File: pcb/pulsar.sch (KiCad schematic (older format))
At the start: 74 parts, among them J1 Conn_01x04, K1 KEYSW, K2 KEYSW, K3 KEYSW, K4 KEYSW, K5 KEYSW, K6 KEYSW, K7 KEYSW, K8 KEYSW, K9 KEYSW, SW1 SW_PUSH, SW2 Rotary_Encoder, SW3 TMHU28, U1 ProMicro

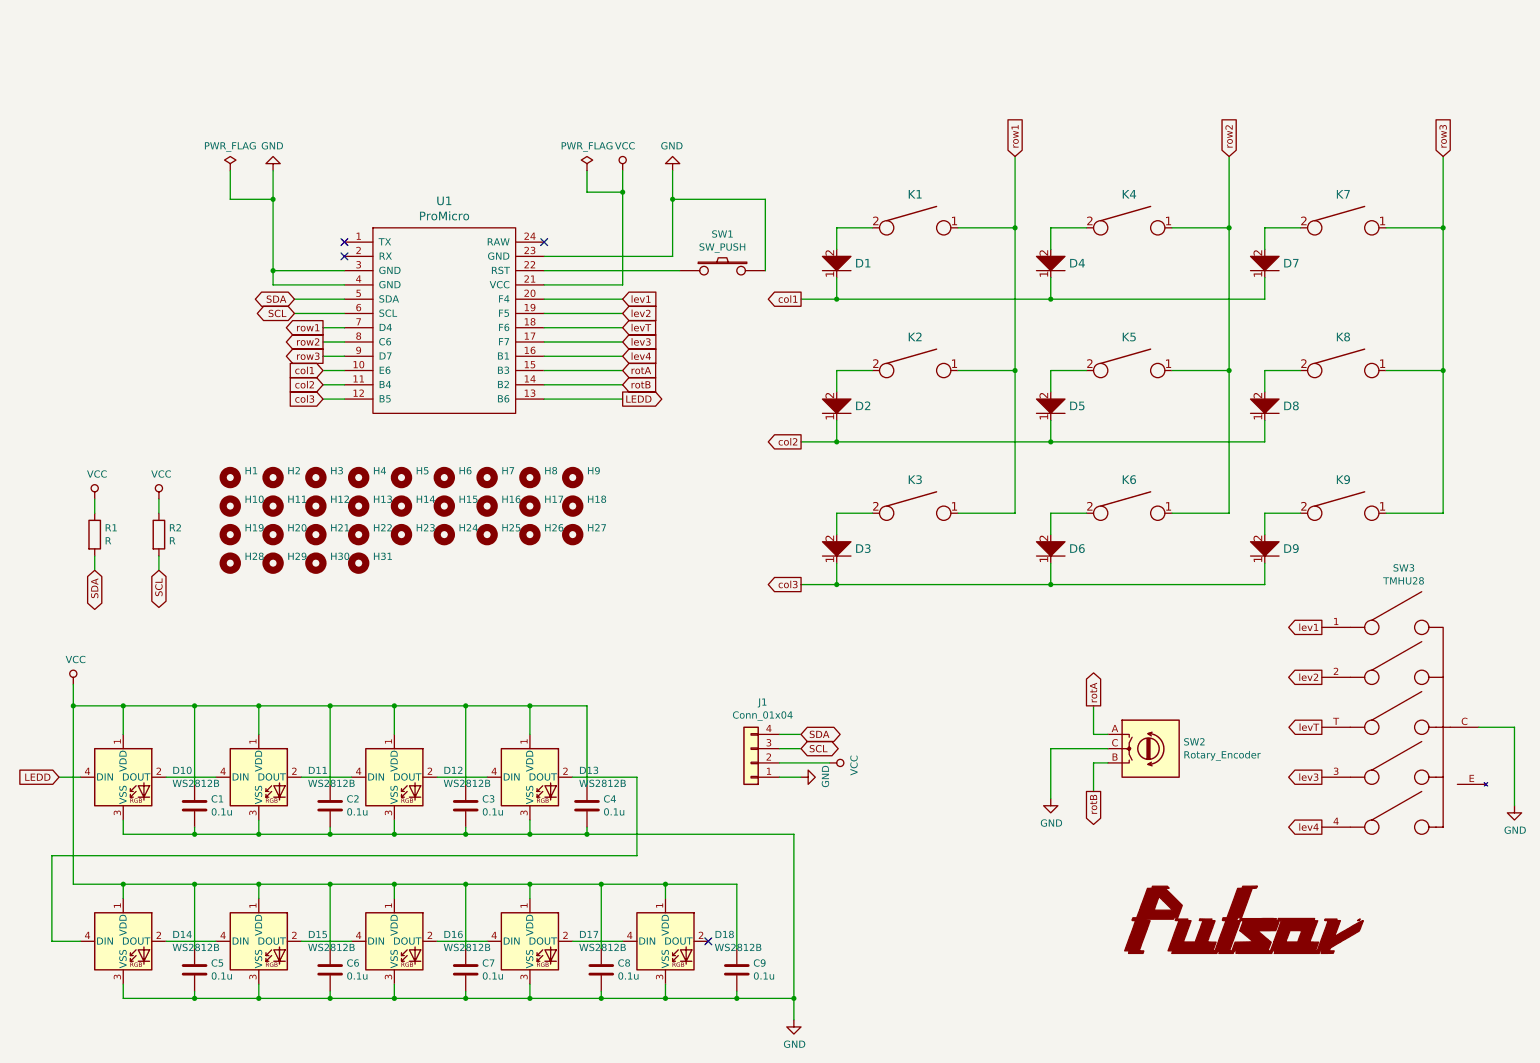
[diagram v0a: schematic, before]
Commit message: update pcb: rev2.0 - 11 keys
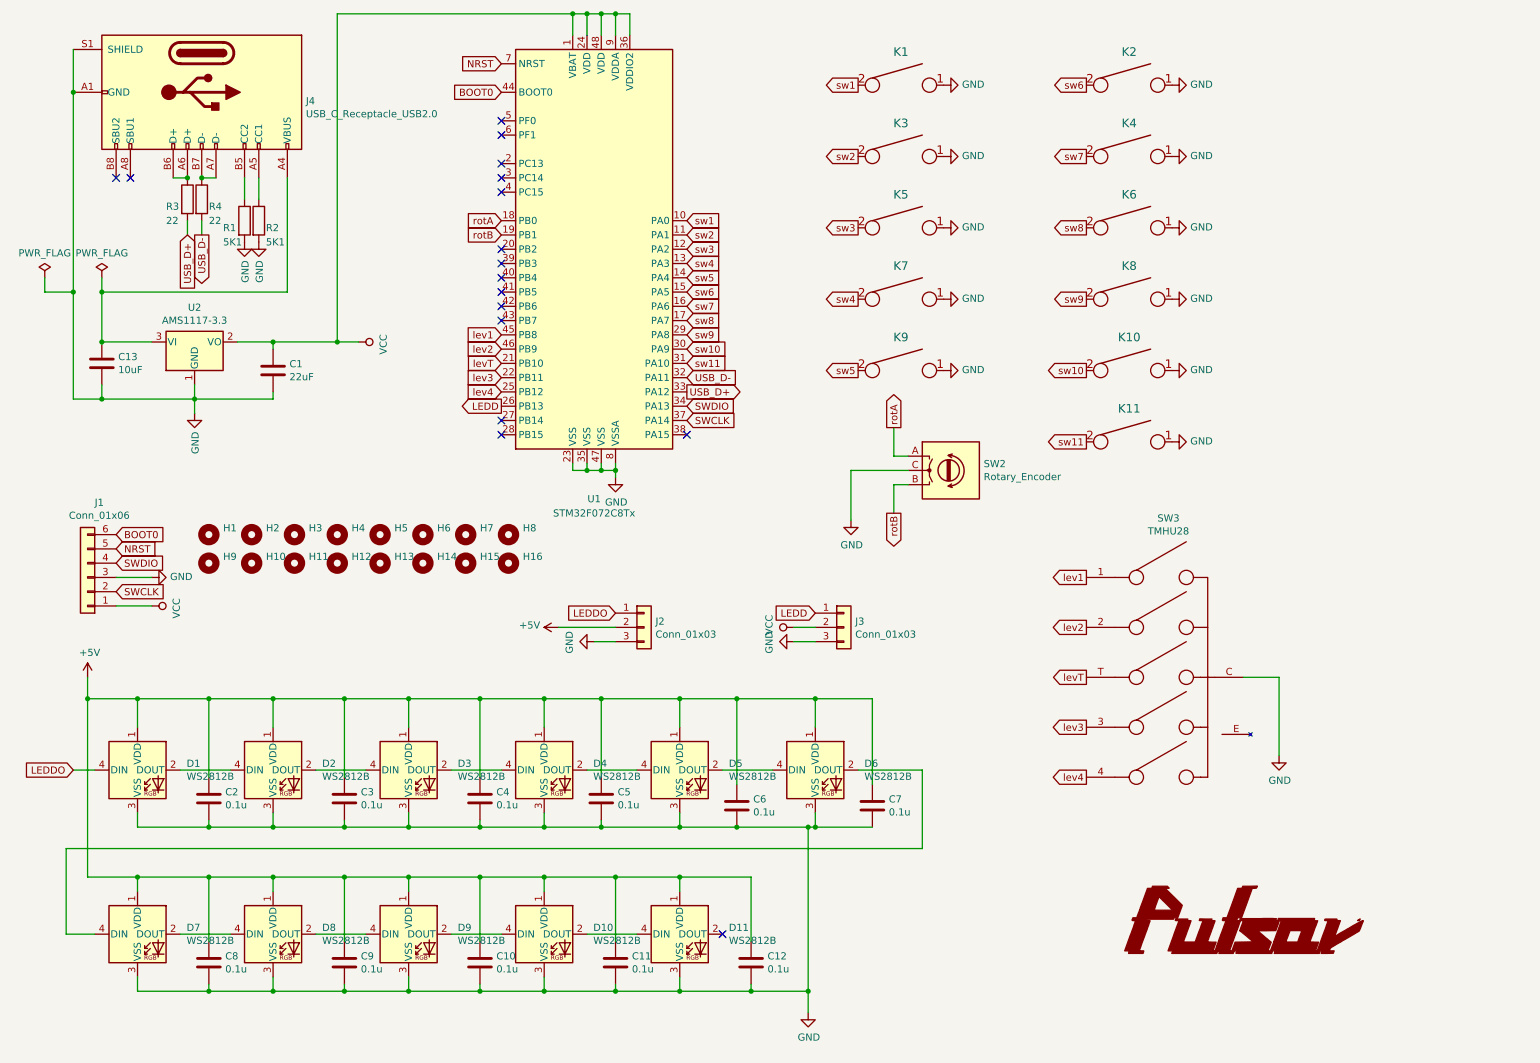
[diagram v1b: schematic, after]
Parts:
- removed D1, D2, D3, D4, D5, D6, D7, D8, D9: D, Diodes_SMD:D_SOD-123, symbol keyboard_parts:D
- removed D12, D13, D14, D15, D16, D17, D18: WS2812B, WS2812-2020:WS2812B-2020, symbol LED:WS2812B
- removed H17, H18, H19, H20, H21, H22, H23, H24, H25, H26, H27, H28, H29, H30, H31: MountingHole, Mounting_Holes:MountingHole_2.2mm_M2, symbol Mechanical:MountingHole
- removed J1: Conn_01x04, Pin_Headers:Pin_Header_Straight_1x04_Pitch2.54mm, symbol Connector_Generic:Conn_01x04
- removed SW1: SW_PUSH, pluser:tactswitch-2lead-6mm, symbol keyboard_parts:SW_PUSH
- removed U1: ProMicro, Keebio-Parts:ArduinoProMicro-ZigZag, symbol promicro:ProMicro
- added C10, C11, C12: 0.1u, Capacitors_SMD:C_0805_HandSoldering, symbol Device:C
- added C13: 10uF, Capacitors_SMD:C_0805_HandSoldering, symbol Device:C
- added D1, D2, D3, D4, D5, D6, D7, D8, D9: WS2812B, LED_SMD:LED_SK6812MINI_PLCC4_3.5x3.5mm_P1.75mm, symbol LED:WS2812B
- added J1: Conn_01x06, Pin_Headers:Pin_Header_Straight_1x06_Pitch2.54mm, symbol Connector_Generic:Conn_01x06
- added J2: Conn_01x03, Pin_Headers:Pin_Header_Straight_1x03_Pitch2.54mm_SMD_Pin1Left, symbol Connector_Generic:Conn_01x03
- added J3: Conn_01x03, pulsar:3pin-zigzag, symbol Connector_Generic:Conn_01x03
- added J4: USB_C_Receptacle_USB2.0, usb-type-c:Mid_Mount-USB_C_HandSoldering, symbol Connector:USB_C_Receptacle_USB2.0
- added K10, K11: KEYSW, keyswitches:Kailh_socket, symbol keyboard_parts:KEYSW
- added R3, R4: 22, Resistors_SMD:R_0805_HandSoldering, symbol Device:R
- added U1: STM32F072C8Tx, Housings_QFP:LQFP-48_7x7mm_Pitch0.5mm, symbol MCU_ST_STM32F0:STM32F072C8Tx
- added U2: AMS1117-3.3, TO_SOT_Packages_SMD:SOT-223-3_TabPin2, symbol Regulator_Linear:AMS1117-3.3
- C1: value 0.1u -> 22uF
- D10, D11: footprint WS2812-2020:WS2812B-2020 -> LED_SMD:LED_SK6812MINI_PLCC4_3.5x3.5mm_P1.75mm
- H1, H2, H3, H4, H5, H6, H7, H9: footprint Mounting_Holes:MountingHole_2.2mm_M2 -> Mounting_Holes:MountingHole_4.3mm_M4
- R1, R2: value R -> 5K1; footprint keyboard_parts:R_1608 -> Resistors_SMD:R_0805_HandSoldering
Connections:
- net SCL is gone; now on net GND: R2.2
- net SDA is gone; now on net GND: R1.2
- net row1 is gone; now on net GND: K1.1, K2.1, K3.1
- net row2 is gone; now on net GND: K4.1, K5.1, K6.1
- net row3 is gone; now on net GND: K7.1, K8.1, K9.1
- net GND: now also C10.2, C11.2, C12.2, C13.2, D1.3 (VSS), D2.3 (VSS), D3.3 (VSS), D4.3 (VSS), D5.3 (VSS), D6.3 (VSS), D7.3 (VSS), D8.3 (VSS), D9.3 (VSS), J1.3 (Pin_3), J2.3 (Pin_3), J3.3 (Pin_3), J4.A1 (GND), J4.A12 (GND), J4.B1 (GND), J4.B12 (GND), J4.S1 (SHIELD), K10.1, K11.1, U1.23 (VSS), U1.35 (VSS), U1.47 (VSS), U1.8 (VSSA), U2.1 (GND)
- net LEDD: now also J3.1 (Pin_1), U1.26 (PB13); no longer D10.4 (DIN)
- net VCC: now also J1.1 (Pin_1), J3.2 (Pin_2), U1.1 (VBAT), U1.24 (VDD), U1.36 (VDDIO2), U1.48 (VDD), U1.9 (VDDA), U2.2 (VO); no longer C2.1, C3.1, C4.1, C5.1, C6.1, C7.1, C8.1, C9.1, D10.1 (VDD), D11.1 (VDD), R1.1, R2.1
- net lev1: now also U1.45 (PB8)
- net lev2: now also U1.46 (PB9)
- net lev3: now also U1.22 (PB11)
- net lev4: now also U1.25 (PB12)
- net levT: now also U1.21 (PB10)
- net rotA: now also U1.18 (PB0)
- net rotB: now also U1.19 (PB1)
- net sw1: now reaches K1.2
- net sw1: now also U1.10 (PA0)
- net sw7: now reaches K4.2
- net sw7: now also U1.16 (PA6)
- net sw6: now reaches K2.2
- net sw6: now also U1.15 (PA5)
- net sw3: now reaches K5.2
- net sw3: now also U1.12 (PA2)
- net sw9: now reaches K8.2
- net sw9: now also U1.29 (PA8)
- net sw4: now reaches K7.2
- net sw4: now also U1.13 (PA3)
- net sw2: now reaches K3.2
- net sw2: now also U1.11 (PA1)
- net sw8: now reaches K6.2
- net sw8: now also U1.17 (PA7)
- net sw5: now reaches K9.2
- net sw5: now also U1.14 (PA4)
- new net: C13.1, J4.A4 (VBUS), J4.A9 (VBUS), J4.B4 (VBUS), J4.B9 (VBUS), U2.3 (VI)
- new net: J4.A5 (CC1), R2.1
- new net: J4.B5 (CC2), R1.1
- new net: D1.2 (DOUT), D2.4 (DIN)
- new net: D2.2 (DOUT), D3.4 (DIN)
- new net: D3.2 (DOUT), D4.4 (DIN)
- new net: D4.2 (DOUT), D5.4 (DIN)
- new net: D7.2 (DOUT), D8.4 (DIN)
- new net: D6.2 (DOUT), D7.4 (DIN)
- new net: D8.2 (DOUT), D9.4 (DIN)
- new net: D10.4 (DIN), D9.2 (DOUT)
- new net: D5.2 (DOUT), D6.4 (DIN)
- new net: J4.A6 (D+), J4.B6 (D+), R3.1
- new net: J4.A7 (D-), J4.B7 (D-), R4.1
- new net +5V: C10.1, C11.1, C12.1, C2.1, C3.1, C4.1, C5.1, C6.1, C7.1, C8.1, C9.1, D1.1 (VDD), D10.1 (VDD), D11.1 (VDD), D2.1 (VDD), D3.1 (VDD), D4.1 (VDD), D5.1 (VDD), D6.1 (VDD), D7.1 (VDD), D8.1 (VDD), D9.1 (VDD), J2.2 (Pin_2)
- new net BOOT0: J1.6 (Pin_6), U1.44 (BOOT0)
- new net LEDDO: D1.4 (DIN), J2.1 (Pin_1)
- new net NRST: J1.5 (Pin_5), U1.7 (NRST)
- new net SWCLK: J1.2 (Pin_2), U1.37 (PA14)
- new net SWDIO: J1.4 (Pin_4), U1.34 (PA13)
- new net USB_D+: R3.2, U1.33 (PA12)
- new net USB_D-: R4.2, U1.32 (PA11)
- new net sw10: K10.2, U1.30 (PA9)
- new net sw11: K11.2, U1.31 (PA10)
- no-connect marks 4 -> 17
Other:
- moved on the sheet: H1, H10, H11, H12, H13, H14, H15, H16, H2, H3, H4, H5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
